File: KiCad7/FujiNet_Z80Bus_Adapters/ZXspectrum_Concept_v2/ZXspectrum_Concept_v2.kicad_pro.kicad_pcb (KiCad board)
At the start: 2 copper layers, 200 x 130 mm, 45 parts, among them IC1 7404N, IC2 74HC32N, IC3 7474N, IC4 74HC08N, IC5 74HC32N, IC6 74HC08N, IC7 74HC32N, IC8 74HC08N, IC9 74HC32N, J1 PinHeader_2.54mm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

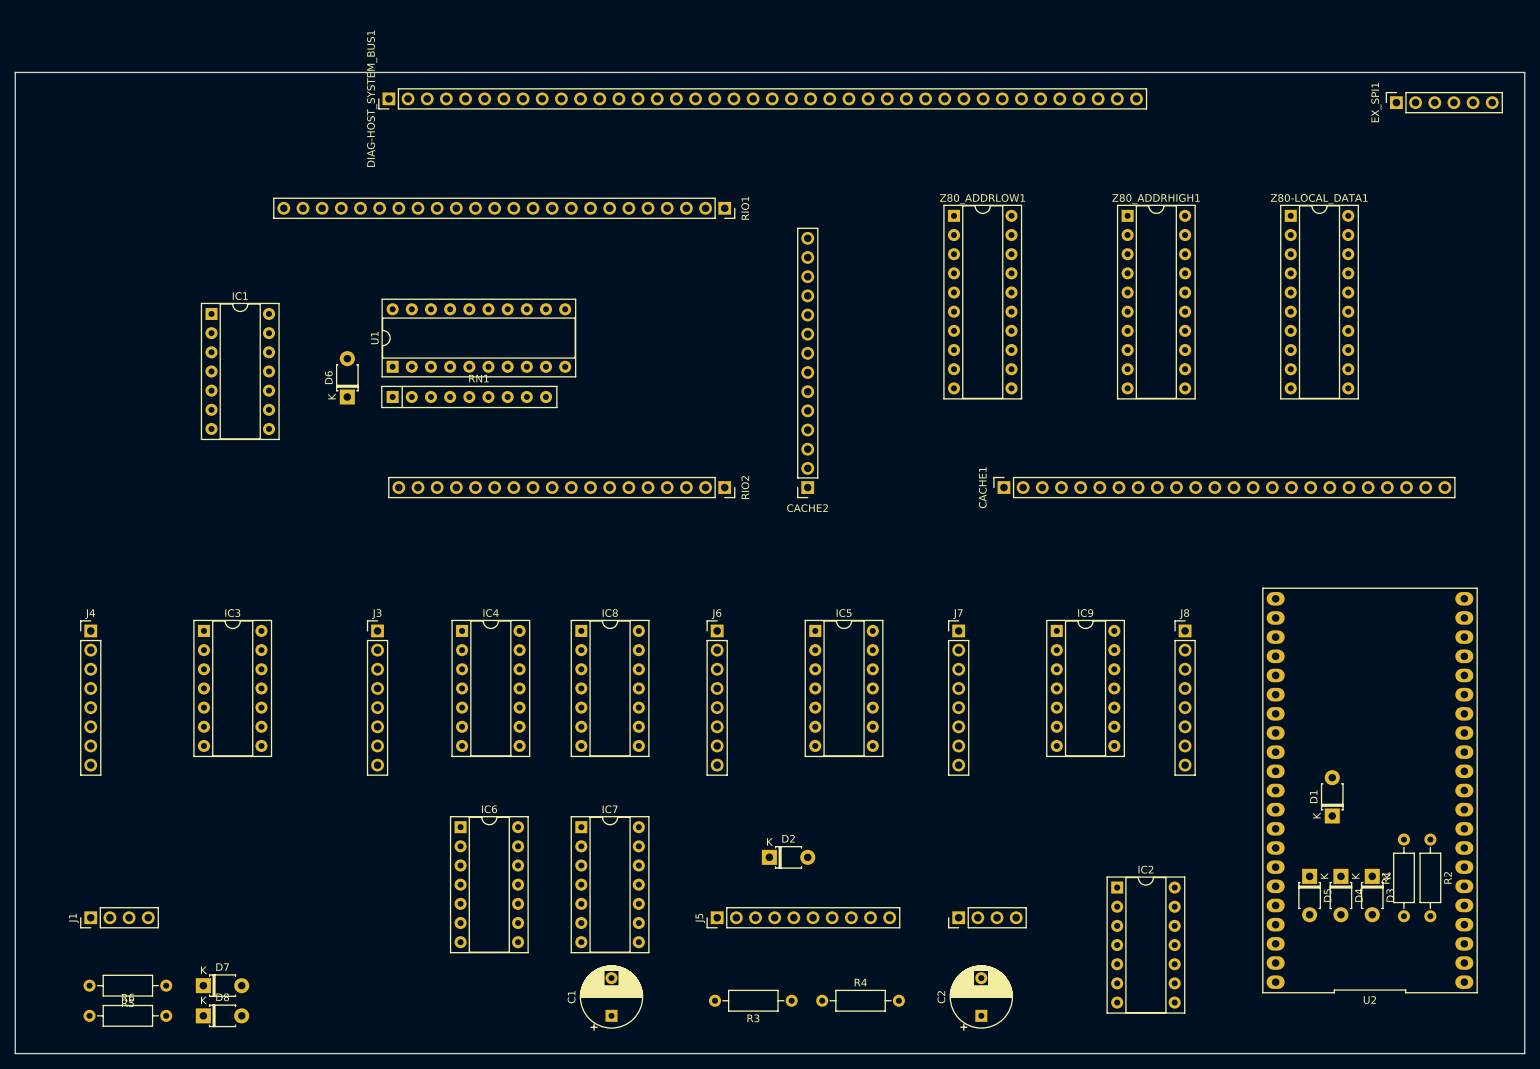
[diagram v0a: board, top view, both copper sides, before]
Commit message: KiCad adapter concept v2 for routing
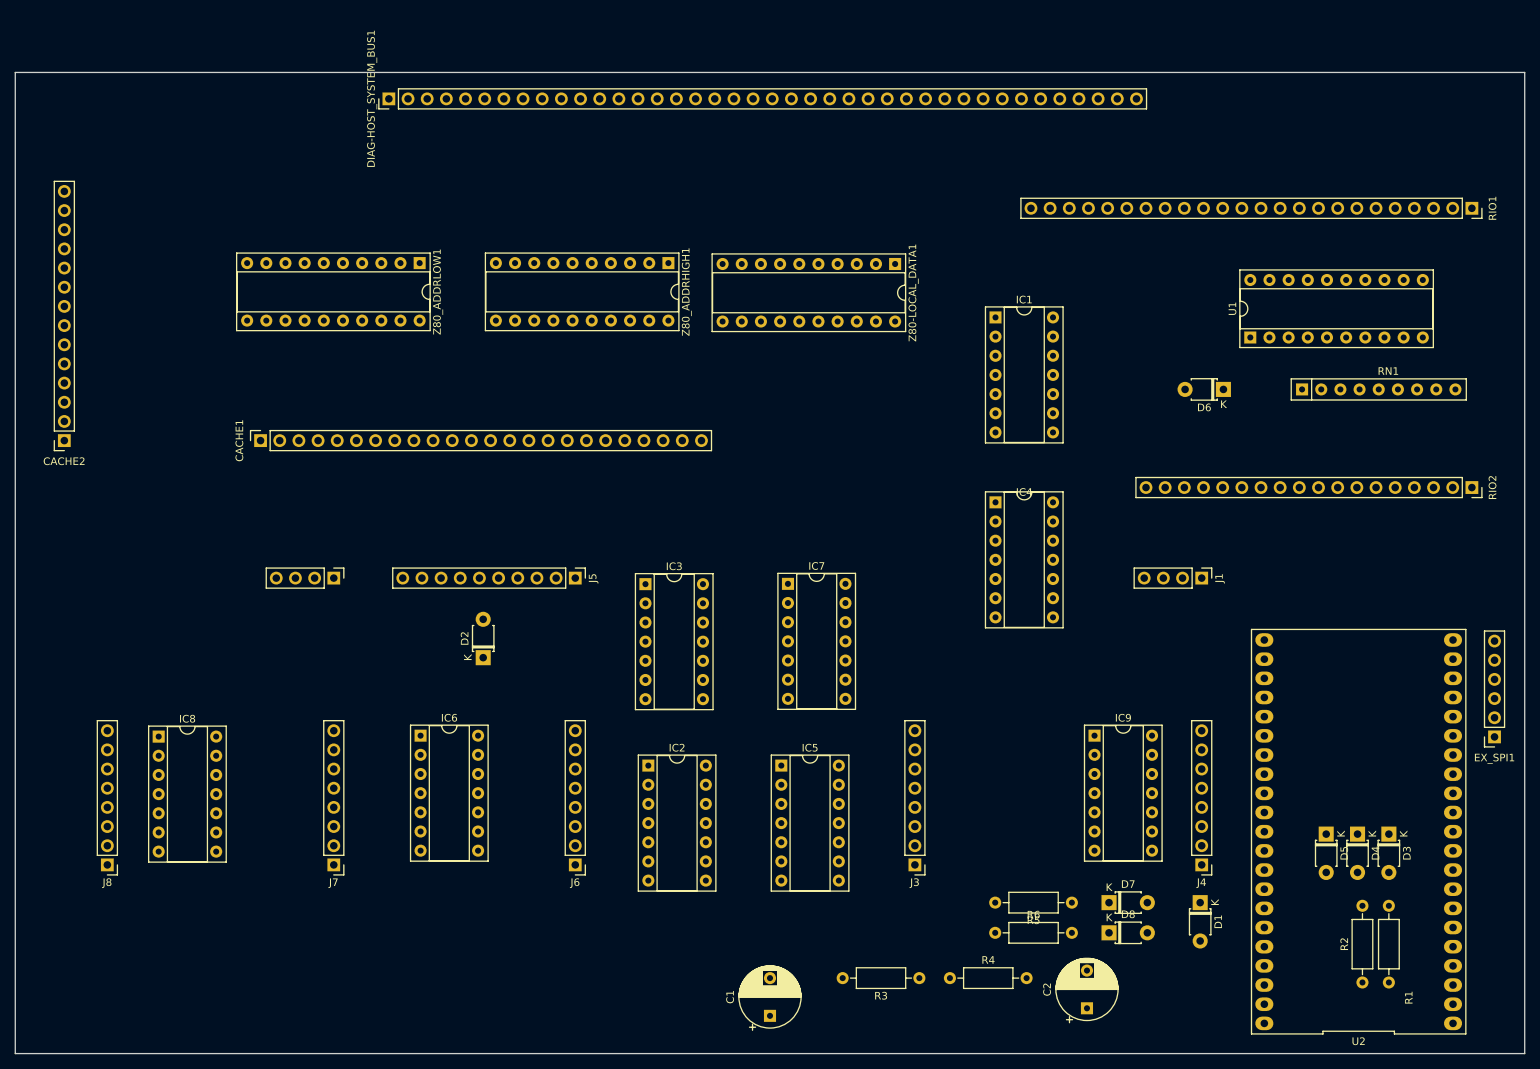
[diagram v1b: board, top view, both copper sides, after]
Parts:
- moved J1 153.9 mm to (199.2, 91.0), turned to -90 degrees
- moved J4 150.4 mm to (199.2, 129.0), turned to 180 degrees
- moved J8 146.1 mm to (54.2, 129.0), turned to 180 degrees
- moved RN1 120.5 mm to (212.5, 66.0)
- moved R5 120.5 mm to (182.0, 134.0)
- moved R6 120.5 mm to (171.8, 138.0)
- moved D7 120.5 mm to (186.9, 134.0)
- moved D8 120.5 mm to (186.9, 138.0)
- moved D6 116.1 mm to (202.1, 66.0), turned to 180 degrees
- moved U1 113.7 mm to (205.6, 59.1)
- moved IC1 103.9 mm to (171.9, 56.5)
- moved RIO1 99.0 mm to (235.0, 42.0)
- moved RIO2 99.0 mm to (235.0, 79.0)
- moved CACHE1 98.7 mm to (74.5, 72.8)
- moved CACHE2 98.7 mm to (48.5, 72.8)
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
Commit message: KiCad Routing  applied to concept adapter PCB
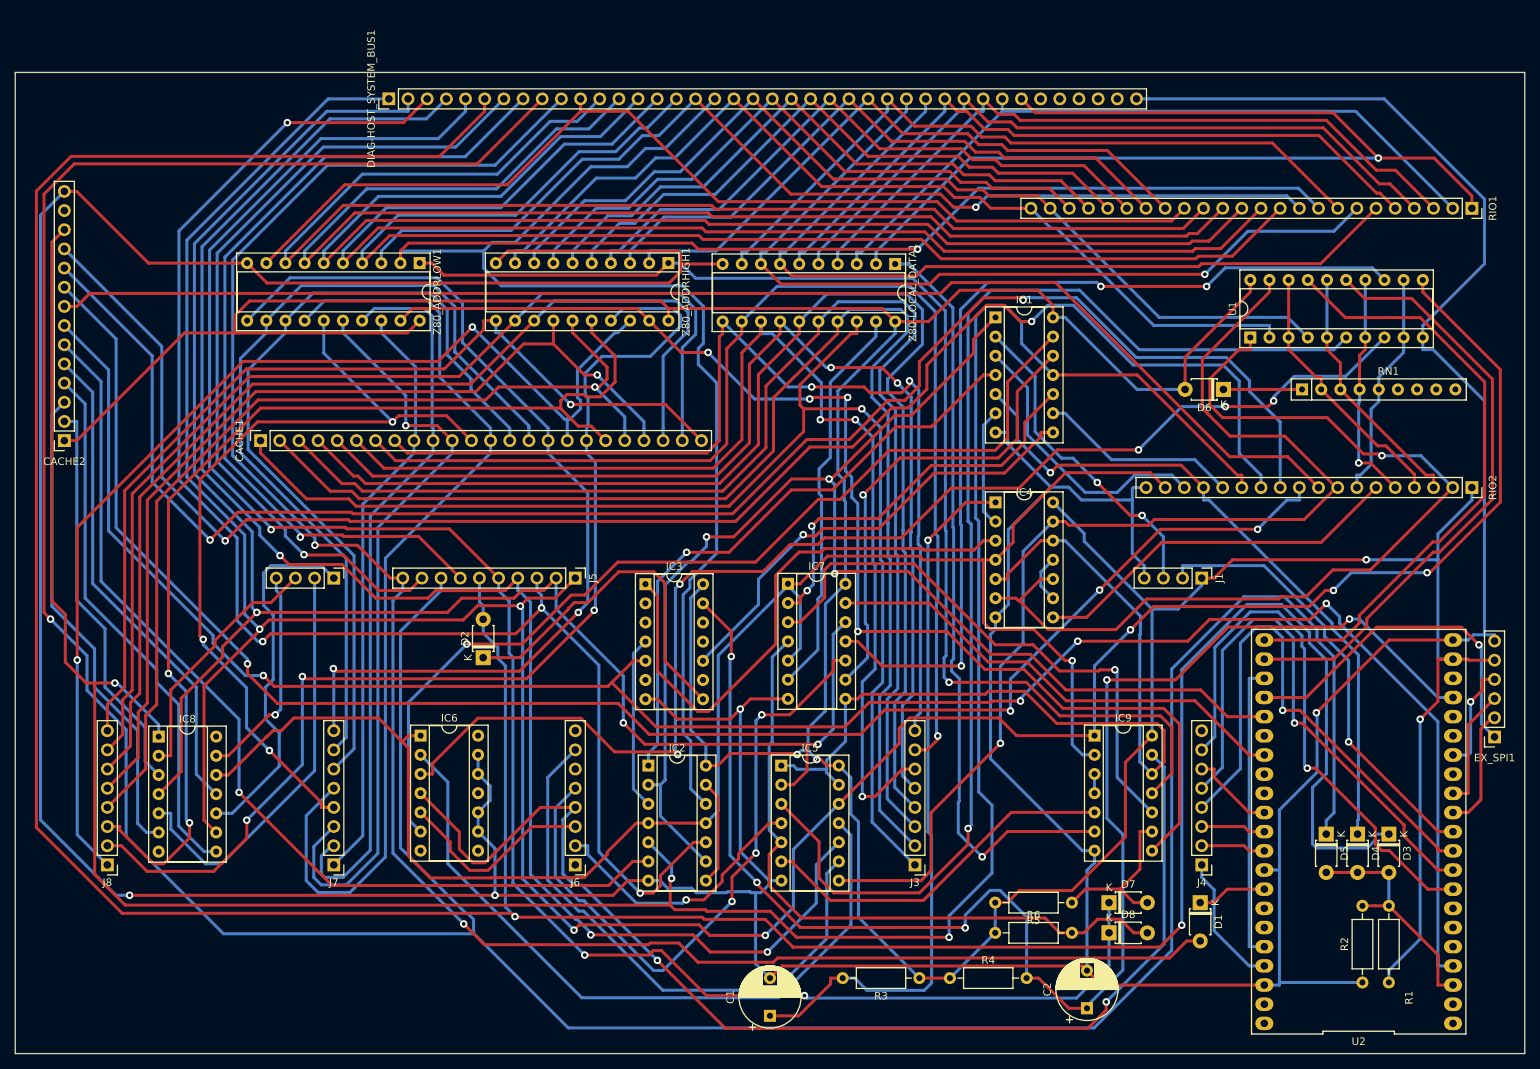
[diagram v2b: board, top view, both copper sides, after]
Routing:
- net GND: track 0.00 -> 765.9 mm, vias 0 -> 4
- net +5V: track 0.00 -> 561.0 mm, vias 0 -> 4
- net /SPI connector/Z80_CONTROL.BUSACK: track 0.00 -> 458.4 mm, vias 0 -> 1
- net /SPI connector/Z80_CONTROL.WAIT: track 0.00 -> 453.3 mm, vias 0 -> 2
- net /SPI connector/Z80_CONTROL.RD: track 0.00 -> 405.4 mm, vias 0 -> 7
- net /CACHE connector/CACHE_DATASTATUS: track 0.00 -> 361.8 mm, vias 0 -> 3
- net /RIO connector/Z80_A0: track 0.00 -> 283.8 mm, vias 0 -> 1
- net /CACHE connector/Z80_HARDLOCK: track 0.00 -> 271.6 mm, vias 0 -> 4
- net /SPI connector/Z80_CONTROL.RESET: track 0.00 -> 259.4 mm, vias 0 -> 2
- net /SPI connector/Z80_CONTROL.BUSRQ: track 0.00 -> 253.8 mm, vias 0 -> 3
- net /SPI connector/Z80_CONTROL.WR: track 0.00 -> 235.7 mm, vias 0 -> 3
- net /GLUE/PERM_Z80_IORQ: track 0.00 -> 234.0 mm, vias 0 -> 1
- net /CACHE connector/CACHE_SEL_1: track 0.00 -> 221.0 mm, vias 0 -> 4
- net /CACHE connector/CACHE_SEL_3: track 0.00 -> 218.1 mm, vias 0 -> 2
- net /CACHE connector/CACHE_SEL_2: track 0.00 -> 217.8 mm, vias 0 -> 2
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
